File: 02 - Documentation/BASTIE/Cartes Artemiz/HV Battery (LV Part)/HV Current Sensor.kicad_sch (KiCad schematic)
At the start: 0 parts

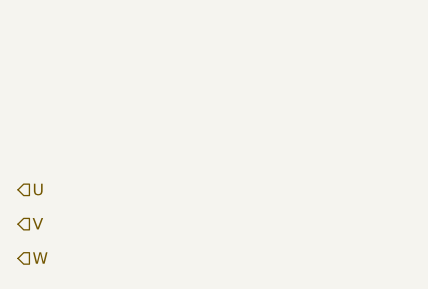
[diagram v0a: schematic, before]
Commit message: Module et Circuit LV Batterie HV
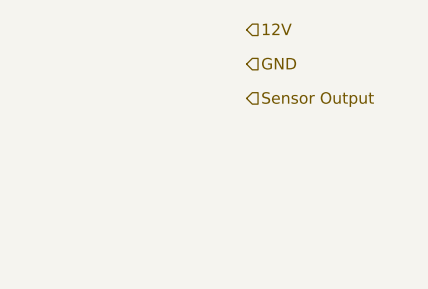
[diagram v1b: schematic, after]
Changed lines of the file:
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@@
 	(generator_version "8.0")
 	(paper "A4")
-	(hierarchical_label "U"
+	(hierarchical_label "GND"
 		(shape input)
-		(at 114.3 83.82 0)
+		(at 139.7 69.85 0)
 		(fields_autoplaced yes)
 		(effects
@@
 		)
 	)
-	(hierarchical_label "W"
+	(hierarchical_label "12V"
 		(shape input)
-		(at 114.3 91.44 0)
+		(at 139.7 66.04 0)
 		(fields_autoplaced yes)
 		(effects
@@
 		)
 	)
-	(hierarchical_label "V"
+	(hierarchical_label "Sensor Output"
 		(shape input)
-		(at 114.3 87.63 0)
+		(at 139.7 73.66 0)
 		(fields_autoplaced yes)
 		(effects
